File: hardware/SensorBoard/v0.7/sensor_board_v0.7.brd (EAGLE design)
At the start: 52.5 x 43 mm, 48 parts, among them J3 USB-MICROB, U1 ATMEGA328P, U10 CCS811, U11 RFM69HW, U2 TSL2561, U4 MPL115A, U5 FT231XS, U7 SHT31, U8 MCP1703/3.3V, U9 MCP1703CB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

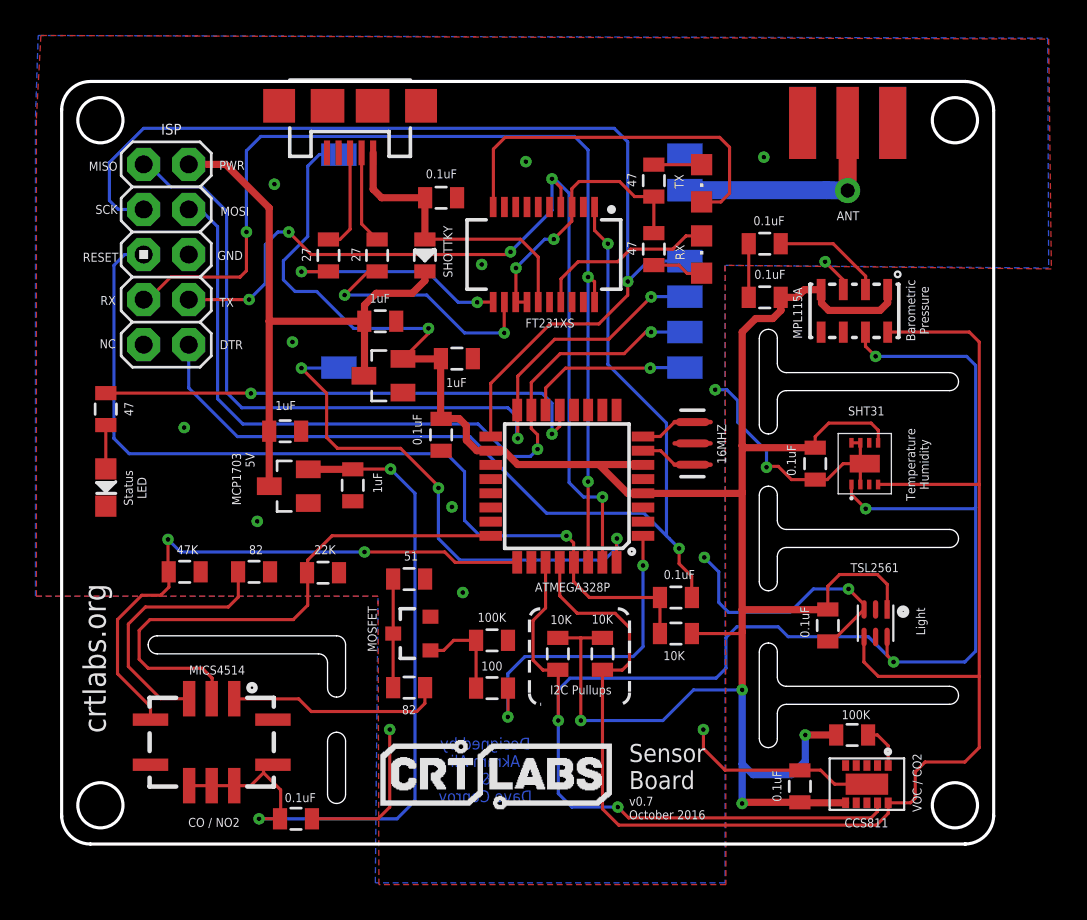
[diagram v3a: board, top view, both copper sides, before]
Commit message: Added loads of GND vias because ¯\_(ツ)_/¯
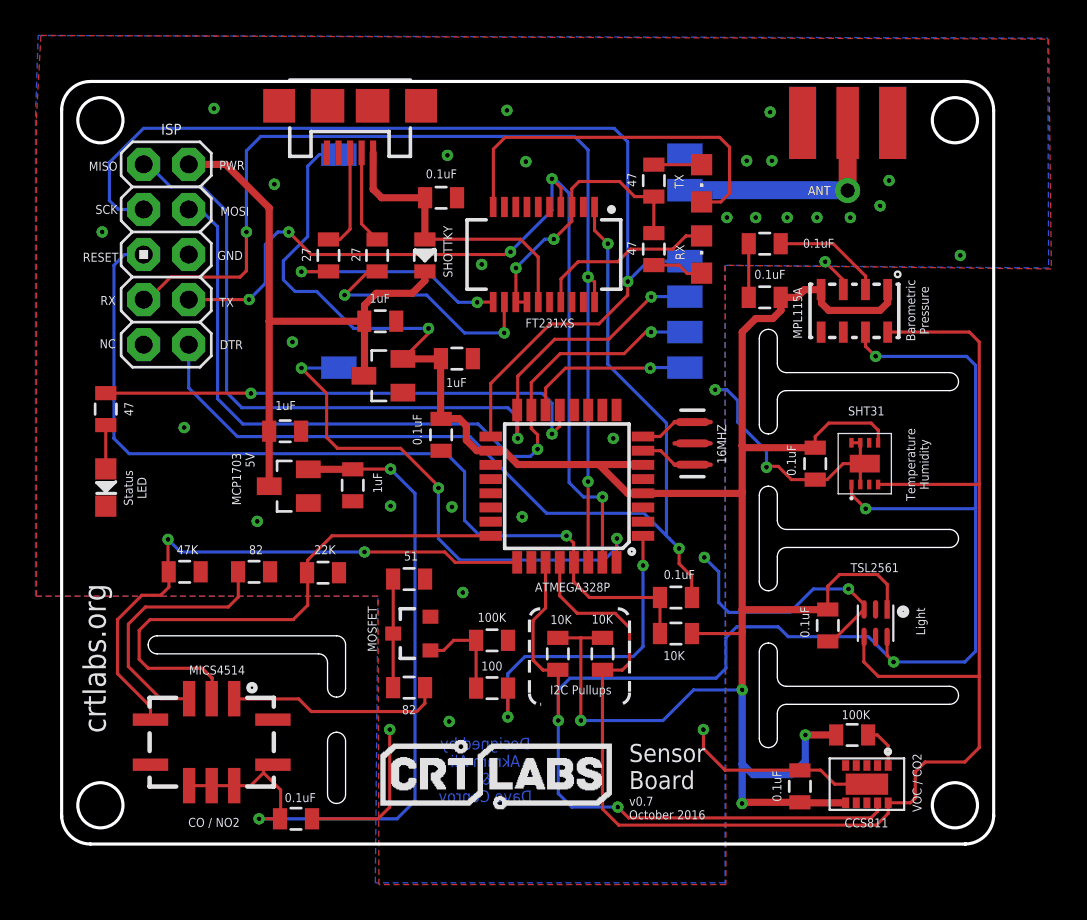
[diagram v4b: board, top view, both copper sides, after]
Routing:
- net GND: vias 16 -> 34
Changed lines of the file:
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@@
 <layer number="118" name="Rect_Pads" color="7" fill="1" visible="yes" active="yes"/>
 <layer number="121" name="_tsilk" color="7" fill="1" visible="yes" active="yes"/>
-<layer number="122" name="_bsilk" color="7" fill="1" visible="no" active="yes"/>
+<layer number="122" name="_bsilk" color="7" fill="1" visible="yes" active="yes"/>
 <layer number="123" name="tTestmark" color="7" fill="1" visible="yes" active="yes"/>
 <layer number="124" name="bTestmark" color="7" fill="1" visible="yes" active="yes"/>
@@
 <wire x1="5.8928" y1="26.2128" x2="5.9944" y2="26.1112" width="0.1778" layer="121"/>
 <wire x1="6.4516" y1="25.7048" x2="5.3848" y2="25.7048" width="0.1778" layer="121"/>
-<text x="48.3616" y="41.6052" size="0.508" layer="121" font="vector" rot="R180">ANT</text>
+<text x="46.736" y="43.0276" size="0.508" layer="121" font="vector" rot="R180">ANT</text>
 <rectangle x1="11.049" y1="8.5598" x2="11.6586" y2="8.6106" layer="122" rot="R180"/>
 <rectangle x1="10.6934" y1="8.5598" x2="10.795" y2="8.6106" layer="122" rot="R180"/>
@@
 </element>
 <element name="C13" library="SparkFun-Passives" package="0805" value="0.1uF" x="43.0276" y="39.7764" smashed="yes" rot="R180">
-<attribute name="VALUE" x="44.1452" y="41.3258" size="0.508" layer="121" font="vector" rot="R180"/>
+<attribute name="VALUE" x="46.9392" y="40.0558" size="0.508" layer="121" font="vector" rot="R180"/>
 </element>
 <element name="C14" library="SparkFun-Passives" package="0805" value="0.1uF" x="43.0276" y="36.7538" smashed="yes" rot="R180">
@@
 <via x="39.624" y="22.098" extent="1-16" drill="0.254" diameter="0.127"/>
 <via x="40.2336" y="31.5468" extent="1-16" drill="0.254" diameter="0.127"/>
-<via x="42.9768" y="44.6532" extent="1-16" drill="0.254" diameter="0.127"/>
+<via x="43.434" y="44.45" extent="1-16" drill="0.254" diameter="0.127"/>
 <via x="29.5656" y="44.3992" extent="1-16" drill="0.254" diameter="0.127"/>
 <via x="46.4312" y="38.7604" extent="1-16" drill="0.254" diameter="0.127"/>
@@
 <wire x1="21.2344" y1="7.366" x2="21.8948" y2="8.0264" width="0.1778" layer="1"/>
 <wire x1="21.8948" y1="8.0264" x2="21.8948" y2="12.3952" width="0.1778" layer="1"/>
+<via x="42.0116" y="44.45" extent="1-16" drill="0.254" diameter="0.127"/>
+<via x="50.038" y="43.3324" extent="1-16" drill="0.254" diameter="0.127"/>
+<via x="49.53" y="41.91" extent="1-16" drill="0.254" diameter="0.127"/>
+<via x="47.8536" y="41.2496" extent="1-16" drill="0.254" diameter="0.127"/>
+<via x="45.974" y="41.2496" extent="1-16" drill="0.254" diameter="0.127"/>
+<via x="44.2976" y="41.2496" extent="1-16" drill="0.254" diameter="0.127"/>
+<via x="42.5196" y="41.2496" extent="1-16" drill="0.254" diameter="0.127"/>
+<via x="40.894" y="41.2496" extent="1-16" drill="0.254" diameter="0.127"/>
+<via x="25.146" y="44.7548" extent="1-16" drill="0.254" diameter="0.127"/>
+<via x="5.6896" y="40.4368" extent="1-16" drill="0.254" diameter="0.127"/>
+<via x="21.9456" y="24.9936" extent="1-16" drill="0.254" diameter="0.127"/>
+<via x="29.3624" y="24.384" extent="1-16" drill="0.254" diameter="0.127"/>
+<via x="34.4932" y="28.8036" extent="1-16" drill="0.254" diameter="0.127"/>
+<via x="25.2476" y="12.8524" extent="1-16" drill="0.254" diameter="0.127"/>
+<via x="54.0512" y="39.116" extent="1-16" drill="0.254" diameter="0.127"/>
+<via x="28.4988" y="47.2948" extent="1-16" drill="0.254" diameter="0.127"/>
+<via x="43.3324" y="47.1932" extent="1-16" drill="0.254" diameter="0.127"/>
+<via x="11.9888" y="47.3964" extent="1-16" drill="0.254" diameter="0.127"/>
 </signal>
 <signal name="VCC">
